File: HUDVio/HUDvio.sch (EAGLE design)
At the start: 48 parts, among them U1 ST_STM32F446RET7, U3 TVP5150AM1PBSR, U4 NEXPERIA_NVT2006, U5 MAXIM_MAX4389, X1 ABRACON_ABM8-27.000MHZ, X2 ABRACON_ABM8-14.31818MHZ

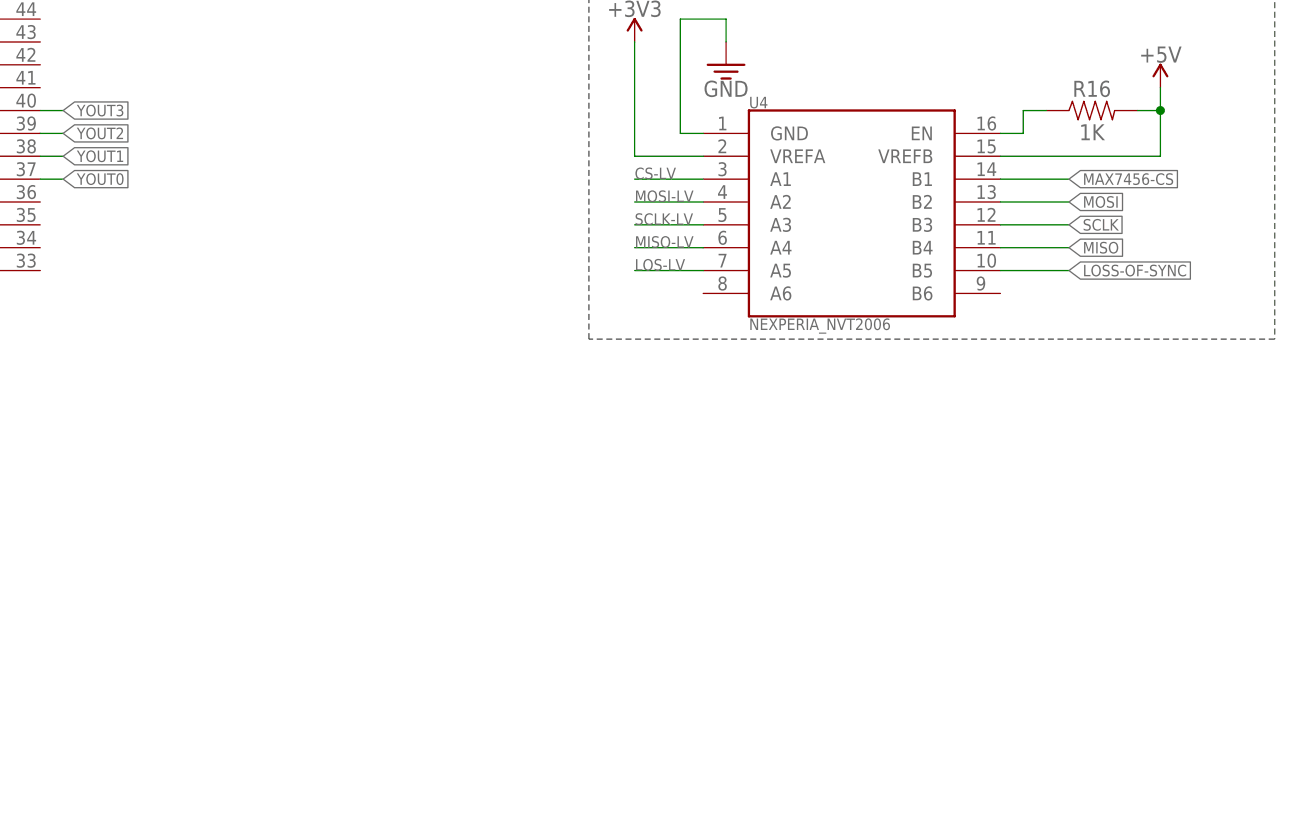
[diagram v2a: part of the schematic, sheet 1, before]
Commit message: Added uSD card
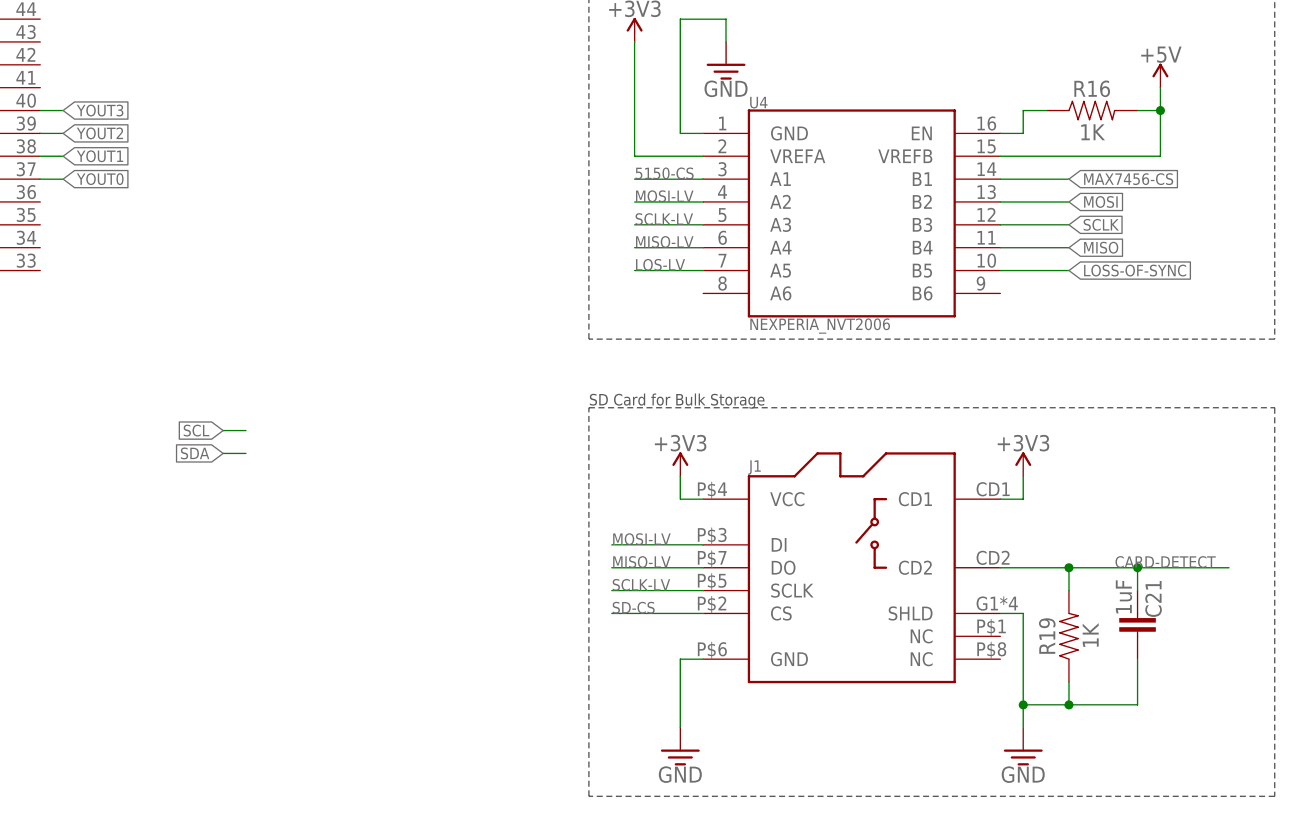
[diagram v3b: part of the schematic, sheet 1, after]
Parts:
- added C21: 1UF_0805, Skyhawkson-Capacitors:1UF_0805
- added J1: (no value), Skyhawkson-Connectors:MOLEX_1040310811
- added R19: 1K_0603, Skyhawkson-Resistors:1K_0603
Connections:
- net CS-LV renamed 5150-CS
- new net CARD-DETECT: C21.1, J1.CD2, R19.2
- new net SD-CS: J1.CS@2
- net +3V3: now also J1.CD1, J1.VCC@4
- net GND: now also C21.2, J1.GND@6, J1.SHLD, R19.1
- net MISO-LV: now also J1.DO@7
- net MOSI-LV: now also J1.DI@3
- net SCLK-LV: now also J1.SCLK@5
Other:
- note added: "SD Card for Bulk Storage"
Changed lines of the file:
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@@
 <part name="R17" library="Skyhawkson-Resistors" library_urn="urn:adsk.eagle:library:23770414" deviceset="75R_0603" device="" package3d_urn="urn:adsk.eagle:package:26071182/3"/>
 <part name="R18" library="Skyhawkson-Resistors" library_urn="urn:adsk.eagle:library:23770414" deviceset="1K_0603" device="" package3d_urn="urn:adsk.eagle:package:26071182/3"/>
+<part name="J1" library="Skyhawkson-Connectors" library_urn="urn:adsk.eagle:library:23896875" deviceset="MOLEX_1040310811" device="" package3d_urn="urn:adsk.eagle:package:24291342/3"/>
+<part name="GND17" library="Skyhawkson-Power Symbols" library_urn="urn:adsk.eagle:library:26071075" deviceset="GND" device=""/>
+<part name="R19" library="Skyhawkson-Resistors" library_urn="urn:adsk.eagle:library:23770414" deviceset="1K_0603" device="" package3d_urn="urn:adsk.eagle:package:26071182/3"/>
+<part name="U$18" library="Skyhawkson-Power Symbols" library_urn="urn:adsk.eagle:library:26071075" deviceset="+3V3" device=""/>
+<part name="C21" library="Skyhawkson-Capacitors" library_urn="urn:adsk.eagle:library:23770361" deviceset="1UF_0805" device="" package3d_urn="urn:adsk.eagle:package:23770363/2"/>
+<part name="U$19" library="Skyhawkson-Power Symbols" library_urn="urn:adsk.eagle:library:26071075" deviceset="+3V3" device=""/>
+<part name="GND18" library="Skyhawkson-Power Symbols" library_urn="urn:adsk.eagle:library:26071075" deviceset="GND" device=""/>
 </parts>
 <sheets>
@@
 due to YCbCr format. Can probably
 adjust in firmware as needed</text>
+<wire x1="172.72" y1="73.66" x2="248.92" y2="73.66" width="0.1524" layer="97" style="shortdash"/>
+<wire x1="248.92" y1="73.66" x2="248.92" y2="30.48" width="0.1524" layer="97" style="shortdash"/>
+<wire x1="248.92" y1="30.48" x2="172.72" y2="30.48" width="0.1524" layer="97" style="shortdash"/>
+<wire x1="172.72" y1="30.48" x2="172.72" y2="73.66" width="0.1524" layer="97" style="shortdash"/>
+<text x="172.72" y="73.914" size="1.27" layer="97">SD Card for Bulk Storage</text>
 </plain>
 <instances>
@@
 <instance part="GND15" gate="G$1" x="187.96" y="111.76" smashed="yes">
 <attribute name="VALUE" x="187.96" y="109.982" size="1.778" layer="96" align="top-center"/>
+</instance>
+<instance part="J1" gate="G$1" x="185.42" y="63.5" smashed="yes">
+<attribute name="NAME" x="190.5" y="66.548" size="1.27" layer="95"/>
+<attribute name="VALUE" x="190.5" y="69.088" size="1.27" layer="96"/>
+</instance>
+<instance part="GND17" gate="G$1" x="220.98" y="35.56" smashed="yes">
+<attribute name="VALUE" x="220.98" y="33.782" size="1.778" layer="96" align="top-center"/>
+</instance>
+<instance part="R19" gate="G$1" x="226.06" y="43.18" smashed="yes" rot="R90">
+<attribute name="NAME" x="224.536" y="48.26" size="1.778" layer="95" font="vector" rot="R90" align="bottom-center"/>
+<attribute name="VAL" x="227.584" y="48.26" size="1.778" layer="96" font="vector" rot="R90" align="top-center"/>
+</instance>
+<instance part="U$18" gate="G$1" x="220.98" y="66.04" smashed="yes">
+<attribute name="VALUE" x="220.98" y="68.834" size="1.778" layer="96" align="bottom-center"/>
+</instance>
+<instance part="C21" gate="G$1" x="233.68" y="53.34" smashed="yes" rot="R270">
+<attribute name="NAME" x="234.569" y="54.61" size="1.778" layer="95" font="vector" rot="R270"/>
+<attribute name="VAL" x="231.267" y="54.61" size="1.778" layer="96" font="vector" rot="R270"/>
+</instance>
+<instance part="U$19" gate="G$1" x="182.88" y="66.04" smashed="yes">
+<attribute name="VALUE" x="182.88" y="68.834" size="1.778" layer="96" align="bottom-center"/>
+</instance>
+<instance part="GND18" gate="G$1" x="182.88" y="35.56" smashed="yes">
+<attribute name="VALUE" x="182.88" y="33.782" size="1.778" layer="96" align="top-center"/>
 </instance>
 </instances>
@@
 <wire x1="177.8" y1="101.6" x2="185.42" y2="101.6" width="0.1524" layer="91"/>
 </segment>
+<segment>
+<pinref part="U$18" gate="G$1" pin="+3V3"/>
+<wire x1="220.98" y1="66.04" x2="220.98" y2="63.5" width="0.1524" layer="91"/>
+<pinref part="J1" gate="G$1" pin="CD1"/>
+<wire x1="220.98" y1="63.5" x2="218.44" y2="63.5" width="0.1524" layer="91"/>
+</segment>
+<segment>
+<pinref part="U$19" gate="G$1" pin="+3V3"/>
+<wire x1="182.88" y1="66.04" x2="182.88" y2="63.5" width="0.1524" layer="91"/>
+<pinref part="J1" gate="G$1" pin="VCC@4"/>
+<wire x1="182.88" y1="63.5" x2="185.42" y2="63.5" width="0.1524" layer="91"/>
+</segment>
 </net>
 <net name="GND" class="0">
@@
 <pinref part="GND15" gate="G$1" pin="GND"/>
 </segment>
-</net>
-<net name="CS-LV" class="0">
+<segment>
+<pinref part="J1" gate="G$1" pin="SHLD"/>
+<wire x1="218.44" y1="50.8" x2="220.98" y2="50.8" width="0.1524" layer="91"/>
+<wire x1="220.98" y1="50.8" x2="220.98" y2="40.64" width="0.1524" layer="91"/>
+<pinref part="GND17" gate="G$1" pin="GND"/>
+<pinref part="R19" gate="G$1" pin="1"/>
+<wire x1="220.98" y1="40.64" x2="220.98" y2="38.1" width="0.1524" layer="91"/>
+<wire x1="226.06" y1="43.18" x2="226.06" y2="40.64" width="0.1524" layer="91"/>
+<wire x1="226.06" y1="40.64" x2="220.98" y2="40.64" width="0.1524" layer="91"/>
+<junction x="220.98" y="40.64"/>
+<pinref part="C21" gate="G$1" pin="2"/>
+<wire x1="233.68" y1="45.72" x2="233.68" y2="40.64" width="0.1524" layer="91"/>
+<wire x1="233.68" y1="40.64" x2="226.06" y2="40.64" width="0.1524" layer="91"/>
+<junction x="226.06" y="40.64"/>
+</segment>
+<segment>
+<pinref part="J1" gate="G$1" pin="GND@6"/>
+<wire x1="185.42" y1="45.72" x2="182.88" y2="45.72" width="0.1524" layer="91"/>
+<wire x1="182.88" y1="45.72" x2="182.88" y2="38.1" width="0.1524" layer="91"/>
+<pinref part="GND18" gate="G$1" pin="GND"/>
+</segment>
+</net>
+<net name="5150-CS" class="0">
 <segment>
 <pinref part="U4" gate="G$1" pin="A1"/>
@@
 <label x="177.8" y="96.52" size="1.27" layer="95"/>
 </segment>
+<segment>
+<wire x1="185.42" y1="58.42" x2="175.26" y2="58.42" width="0.1524" layer="91"/>
+<label x="175.26" y="58.42" size="1.27" layer="95"/>
+<pinref part="J1" gate="G$1" pin="DI@3"/>
+</segment>
 </net>
 <net name="SCLK-LV" class="0">
@@
 <label x="177.8" y="93.98" size="1.27" layer="95"/>
 </segment>
+<segment>
+<wire x1="185.42" y1="53.34" x2="175.26" y2="53.34" width="0.1524" layer="91"/>
+<label x="175.26" y="53.34" size="1.27" layer="95"/>
+<pinref part="J1" gate="G$1" pin="SCLK@5"/>
+</segment>
 </net>
 <net name="MISO-LV" class="0">
@@
 <label x="177.8" y="91.44" size="1.27" layer="95"/>
 </segment>
+<segment>
+<wire x1="185.42" y1="55.88" x2="175.26" y2="55.88" width="0.1524" layer="91"/>
+<label x="175.26" y="55.88" size="1.27" layer="95"/>
+<pinref part="J1" gate="G$1" pin="DO@7"/>
+</segment>
 </net>
 <net name="LOS-LV" class="0">
@@
 </segment>
 </net>
+<net name="CARD-DETECT" class="0">
+<segment>
+<pinref part="J1" gate="G$1" pin="CD2"/>
+<pinref part="R19" gate="G$1" pin="2"/>
+<wire x1="218.44" y1="55.88" x2="226.06" y2="55.88" width="0.1524" layer="91"/>
+<wire x1="226.06" y1="55.88" x2="226.06" y2="53.34" width="0.1524" layer="91"/>
+<wire x1="226.06" y1="55.88" x2="233.68" y2="55.88" width="0.1524" layer="91"/>
+<junction x="226.06" y="55.88"/>
+<pinref part="C21" gate="G$1" pin="1"/>
+<wire x1="233.68" y1="55.88" x2="233.68" y2="53.34" width="0.1524" layer="91"/>
+<wire x1="233.68" y1="55.88" x2="243.84" y2="55.88" width="0.1524" layer="91"/>
+<junction x="233.68" y="55.88"/>
+<label x="231.14" y="55.88" size="1.27" layer="95"/>
+</segment>
+</net>
+<net name="SD-CS" class="0">
+<segment>
+<pinref part="J1" gate="G$1" pin="CS@2"/>
+<wire x1="185.42" y1="50.8" x2="175.26" y2="50.8" width="0.1524" layer="91"/>
+<label x="175.26" y="50.8" size="1.27" layer="95"/>
+</segment>
+</net>
+<net name="SDA" class="0">
+<segment>
+<wire x1="134.62" y1="68.58" x2="132.08" y2="68.58" width="0.1524" layer="91"/>
+<label x="132.08" y="68.58" size="1.27" layer="95" rot="MR0" xref="yes"/>
+</segment>
+</net>
+<net name="SCL" class="0">
+<segment>
+<wire x1="134.62" y1="71.12" x2="132.08" y2="71.12" width="0.1524" layer="91"/>
+<label x="132.08" y="71.12" size="1.27" layer="95" rot="MR0" xref="yes"/>
+</segment>
+</net>

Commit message: Assigned more pins
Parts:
- added R20, R21: 2K2_0603, Skyhawkson-Resistors:2K2_0603
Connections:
- net +3V3: now also R20.2, R21.2
- net ACTIVE-VID: now also U1.PC12@53
- net FID/GLCO: now also U1.PC10@51
- net SCL: now also R20.1
- net SDA: now also R21.1
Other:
- note added: "ACTIVE-VID and GLCO may not be used but I'm attaching them to extra DCMI lines in case. In 8-bit YCbCr mode, the extra will simply be ignored anyway."
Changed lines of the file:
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@@
 <part name="U$19" library="Skyhawkson-Power Symbols" library_urn="urn:adsk.eagle:library:26071075" deviceset="+3V3" device=""/>
 <part name="GND18" library="Skyhawkson-Power Symbols" library_urn="urn:adsk.eagle:library:26071075" deviceset="GND" device=""/>
+<part name="R20" library="Skyhawkson-Resistors" library_urn="urn:adsk.eagle:library:23770414" deviceset="2K2_0603" device="" package3d_urn="urn:adsk.eagle:package:26071182/3"/>
+<part name="R21" library="Skyhawkson-Resistors" library_urn="urn:adsk.eagle:library:23770414" deviceset="2K2_0603" device="" package3d_urn="urn:adsk.eagle:package:26071182/3"/>
+<part name="U$20" library="Skyhawkson-Power Symbols" library_urn="urn:adsk.eagle:library:26071075" deviceset="+3V3" device=""/>
+<part name="U$21" library="Skyhawkson-Power Symbols" library_urn="urn:adsk.eagle:library:26071075" deviceset="+3V3" device=""/>
 </parts>
 <sheets>
@@
 <wire x1="172.72" y1="30.48" x2="172.72" y2="73.66" width="0.1524" layer="97" style="shortdash"/>
 <text x="172.72" y="73.914" size="1.27" layer="97">SD Card for Bulk Storage</text>
+<text x="99.06" y="152.4" size="1.27" layer="97">ACTIVE-VID and GLCO may not be used
+but I'm attaching them to extra DCMI
+lines in case. In 8-bit YCbCr mode, the extra
+will simply be ignored anyway.</text>
 </plain>
 <instances>
@@
 <instance part="GND18" gate="G$1" x="182.88" y="35.56" smashed="yes">
 <attribute name="VALUE" x="182.88" y="33.782" size="1.778" layer="96" align="top-center"/>
+</instance>
+<instance part="R20" gate="G$1" x="137.16" y="73.66" smashed="yes" rot="R90">
+<attribute name="NAME" x="135.636" y="78.74" size="1.778" layer="95" font="vector" rot="R90" align="bottom-center"/>
+<attribute name="VAL" x="138.684" y="78.74" size="1.778" layer="96" font="vector" rot="R90" align="top-center"/>
+</instance>
+<instance part="R21" gate="G$1" x="147.32" y="73.66" smashed="yes" rot="R90">
+<attribute name="NAME" x="145.796" y="78.74" size="1.778" layer="95" font="vector" rot="R90" align="bottom-center"/>
+<attribute name="VAL" x="148.844" y="78.74" size="1.778" layer="96" font="vector" rot="R90" align="top-center"/>
+</instance>
+<instance part="U$20" gate="G$1" x="147.32" y="86.36" smashed="yes">
+<attribute name="VALUE" x="147.32" y="89.154" size="1.778" layer="96" align="bottom-center"/>
+</instance>
+<instance part="U$21" gate="G$1" x="137.16" y="86.36" smashed="yes">
+<attribute name="VALUE" x="137.16" y="89.154" size="1.778" layer="96" align="bottom-center"/>
 </instance>
 </instances>
@@
 <pinref part="U4" gate="G$1" pin="B5"/>
 </segment>
+<segment>
+<label x="132.08" y="33.02" size="1.27" layer="95" rot="R180" xref="yes"/>
+<wire x1="134.62" y1="33.02" x2="132.08" y2="33.02" width="0.1524" layer="91"/>
+</segment>
 </net>
 <net name="N$13" class="0">
@@
 <pinref part="J1" gate="G$1" pin="VCC@4"/>
 <wire x1="182.88" y1="63.5" x2="185.42" y2="63.5" width="0.1524" layer="91"/>
+</segment>
+<segment>
+<pinref part="R21" gate="G$1" pin="2"/>
+<wire x1="147.32" y1="83.82" x2="147.32" y2="86.36" width="0.1524" layer="91"/>
+<pinref part="U$20" gate="G$1" pin="+3V3"/>
+</segment>
+<segment>
+<pinref part="R20" gate="G$1" pin="2"/>
+<wire x1="137.16" y1="83.82" x2="137.16" y2="86.36" width="0.1524" layer="91"/>
+<pinref part="U$21" gate="G$1" pin="+3V3"/>
 </segment>
 </net>
@@
 <label x="177.8" y="99.06" size="1.27" layer="95"/>
 </segment>
+<segment>
+<wire x1="129.54" y1="60.96" x2="121.92" y2="60.96" width="0.1524" layer="91"/>
+<label x="121.92" y="60.96" size="1.27" layer="95"/>
+</segment>
 </net>
 <net name="MOSI-LV" class="0">
@@
 <pinref part="J1" gate="G$1" pin="DI@3"/>
 </segment>
+<segment>
+<wire x1="129.54" y1="58.42" x2="121.92" y2="58.42" width="0.1524" layer="91"/>
+<label x="121.92" y="58.42" size="1.27" layer="95"/>
+</segment>
 </net>
 <net name="SCLK-LV" class="0">
@@
 <pinref part="J1" gate="G$1" pin="SCLK@5"/>
 </segment>
+<segment>
+<wire x1="129.54" y1="55.88" x2="121.92" y2="55.88" width="0.1524" layer="91"/>
+<label x="121.92" y="55.88" size="1.27" layer="95"/>
+</segment>
 </net>
 <net name="MISO-LV" class="0">
@@
 <pinref part="J1" gate="G$1" pin="DO@7"/>
 </segment>
+<segment>
+<wire x1="129.54" y1="53.34" x2="121.92" y2="53.34" width="0.1524" layer="91"/>
+<label x="121.92" y="53.34" size="1.27" layer="95"/>
+</segment>
 </net>
 <net name="LOS-LV" class="0">
@@
 <wire x1="185.42" y1="88.9" x2="177.8" y2="88.9" width="0.1524" layer="91"/>
 <label x="177.8" y="88.9" size="1.27" layer="95"/>
+</segment>
+<segment>
+<wire x1="129.54" y1="50.8" x2="121.92" y2="50.8" width="0.1524" layer="91"/>
+<label x="121.92" y="50.8" size="1.27" layer="95"/>
 </segment>
 </net>
@@
 <label x="175.26" y="50.8" size="1.27" layer="95"/>
 </segment>
+<segment>
+<wire x1="132.08" y1="63.5" x2="121.92" y2="63.5" width="0.1524" layer="91"/>
+<label x="121.92" y="63.5" size="1.27" layer="95"/>
+</segment>
 </net>
 <net name="SDA" class="0">
 <segment>
-<wire x1="134.62" y1="68.58" x2="132.08" y2="68.58" width="0.1524" layer="91"/>
 <label x="132.08" y="68.58" size="1.27" layer="95" rot="MR0" xref="yes"/>
+<pinref part="R21" gate="G$1" pin="1"/>
+<wire x1="147.32" y1="73.66" x2="147.32" y2="68.58" width="0.1524" layer="91"/>
+<wire x1="147.32" y1="68.58" x2="132.08" y2="68.58" width="0.1524" layer="91"/>
+<wire x1="147.32" y1="68.58" x2="157.48" y2="68.58" width="0.1524" layer="91"/>
+<junction x="147.32" y="68.58"/>
 </segment>
 </net>
 <net name="SCL" class="0">
 <segment>
-<wire x1="134.62" y1="71.12" x2="132.08" y2="71.12" width="0.1524" layer="91"/>
 <label x="132.08" y="71.12" size="1.27" layer="95" rot="MR0" xref="yes"/>
-</segment>
-</net>
+<wire x1="132.08" y1="71.12" x2="137.16" y2="71.12" width="0.1524" layer="91"/>
+<pinref part="R20" gate="G$1" pin="1"/>
+<wire x1="137.16" y1="71.12" x2="137.16" y2="73.66" width="0.1524" layer="91"/>
+<wire x1="137.16" y1="71.12" x2="157.48" y2="71.12" width="0.1524" layer="91"/>
+<junction x="137.16" y="71.12"/>
+</segment>
+</net>
+<net name="ACTIVE-VID" class="0">
+<segment>
+<label x="83.82" y="147.32" size="1.27" layer="95" rot="R90" xref="yes"/>
+<pinref part="U1" gate="G$1" pin="PC12@53"/>
+<wire x1="83.82" y1="147.32" x2="83.82" y2="144.78" width="0.1524" layer="91"/>
+</segment>
+</net>
+<net name="FID/GLCO" class="0">
+<segment>
+<wire x1="88.9" y1="144.78" x2="88.9" y2="147.32" width="0.1524" layer="91"/>
+<label x="88.9" y="147.32" size="1.27" layer="95" rot="R90" xref="yes"/>
+<pinref part="U1" gate="G$1" pin="PC10@51"/>
+</segment>
+</net>

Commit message: Added 3rd sheet
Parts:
- added C22, C23, C24, C25, C26: 1UF_0805, Skyhawkson-Capacitors:1UF_0805
- added R22: 1K_0603, Skyhawkson-Resistors:1K_0603
- added S1: C&K_PTS815, Skyhawkson-Miscellaneous:C&K_PTS815
- added U6: MIC_MIC5504-1.8, Skyhawkson-Power:MIC_MIC5504-1.8
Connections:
- new net N$16: S1.2, U1.!RST!@7
- new net N$17: R22.1, S1.1
- new net N$18: C26.2, S1.3
- net +3V3: now also C22.1, C23.1, C24.1, C25.1, C26.1, R22.2, U1.VDD@19, U1.VDD@32, U1.VDD@48, U1.VDD@64, U1.VDDA/VREF+@13
- net 5150-CS: now also U1.PB12@33
- net BLU: now also U1.PA2@16
- net GND: now also C22.2, C23.2, C24.2, C25.2, S1.4, U1.GND@18, U1.GND@31, U1.GND@47, U1.GND@63, U1.GNDA/VREF-@12
- net GRE: now also U1.PA1@15
- net LOS-LV: now also U1.PC0@8
- net MISO-LV: now also U1.PB14@35
- net MOSI-LV: now also U1.PB15@36
- net RED: now also U1.PA0@14
- net SCL: now also U1.PB10@29
- net SCLK-LV: now also U1.PB13@34
- net SD-CS: now also U1.PB4@56
- net SDA: now also U1.PB3@55
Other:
- note added: "Tying I2C to I2C2 on pins 55 and 29"
- note added: "Using PWM on TIM2 CH1-3"
- note added: "Using SPI2 for 5150 and SD Card"
